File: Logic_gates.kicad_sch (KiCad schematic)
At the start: 3 parts, among them U7 MC74VHC1G04, U8 MC74VHC1G04, U9 74HC08D.653

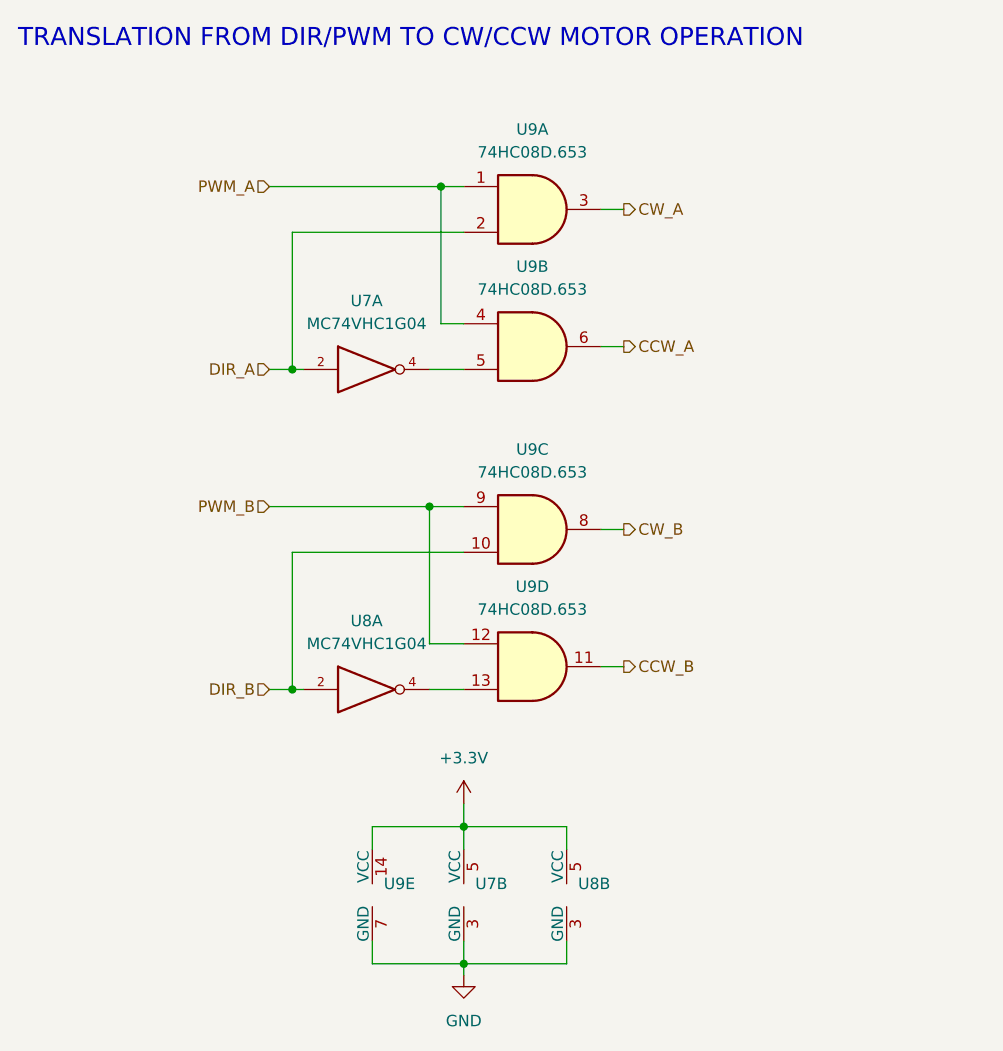
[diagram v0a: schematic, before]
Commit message: added pull-ups to the logic gates
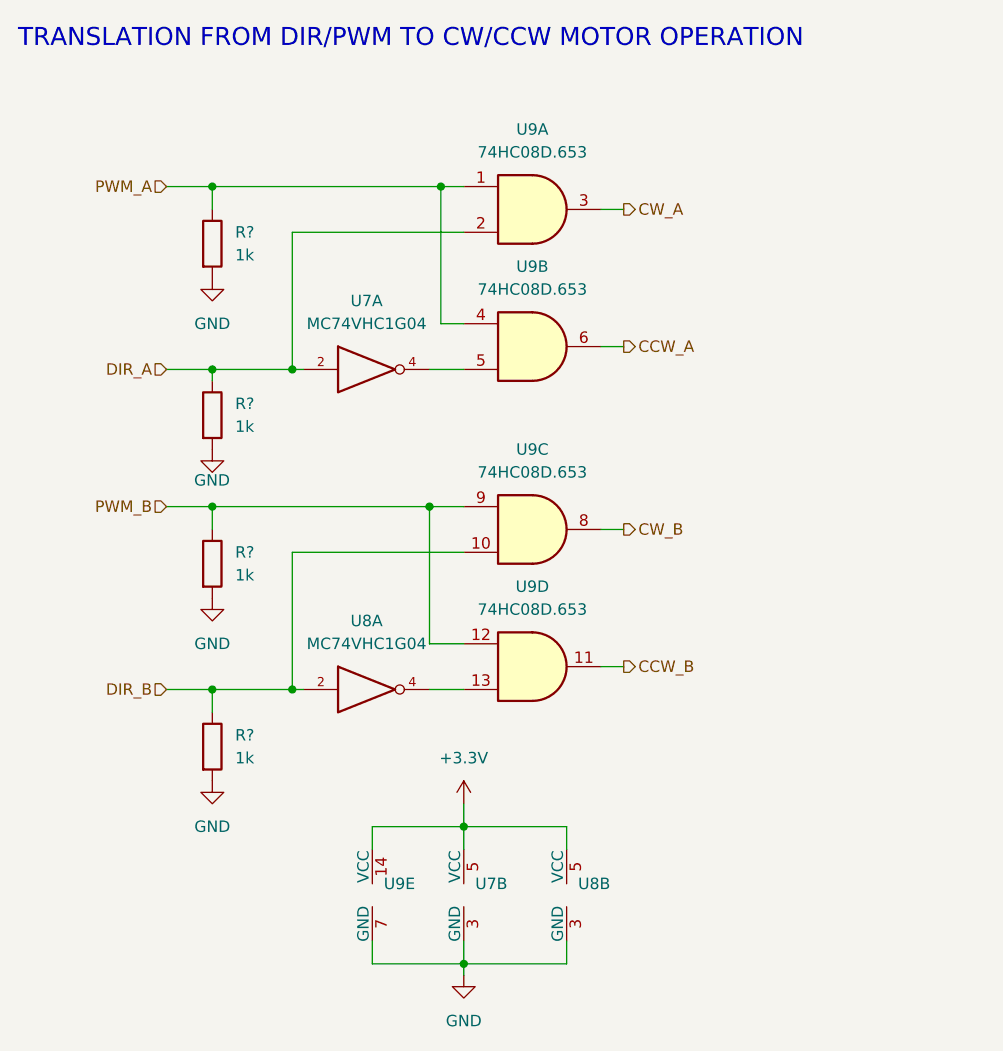
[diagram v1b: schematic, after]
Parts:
- added R? (x4): 1k, Resistor_SMD:R_0603_1608Metric_Pad0.98x0.95mm_HandSolder, symbol Device:R
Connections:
- net DIR_A: now also R?.1
- net DIR_B: now also R?.1
- net GND: now also R?.2, R?.2, R?.2, R?.2
- net PWM_A: now also R?.1
- net PWM_B: now also R?.1
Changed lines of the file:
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@@
   (junction (at 138.43 50.8) (diameter 0) (color 0 0 0 0)
   )
+  (junction (at 113.03 50.8) (diameter 0) (color 0 0 0 0)
+  )
   (junction (at 140.97 137.16) (diameter 0) (color 0 0 0 0)
   )
+  (junction (at 113.03 71.12) (diameter 0) (color 0 0 0 0)
+  )
   (junction (at 121.92 71.12) (diameter 0) (color 0 0 0 0)
   )
   (junction (at 140.97 121.92) (diameter 0) (color 0 0 0 0)
   )
+  (junction (at 113.03 86.36) (diameter 0) (color 0 0 0 0)
+  )
+  (junction (at 113.03 106.68) (diameter 0) (color 0 0 0 0)
+  )
   (junction (at 121.92 106.68) (diameter 0) (color 0 0 0 0)
   )
@@
     (stroke (width 0) (type default) (color 0 0 0 0))
   )
-  (wire (pts (xy 119.38 106.68) (xy 121.92 106.68))
+  (wire (pts (xy 107.95 106.68) (xy 113.03 106.68))
+    (stroke (width 0) (type default) (color 0 0 0 0))
+  )
+  (wire (pts (xy 113.03 106.68) (xy 121.92 106.68))
     (stroke (width 0) (type default) (color 0 0 0 0))
   )
@@
     (stroke (width 0) (type default) (color 0 0 0 0))
   )
+  (wire (pts (xy 113.03 72.39) (xy 113.03 71.12))
+    (stroke (width 0) (type default) (color 0 0 0 0))
+  )
+  (wire (pts (xy 113.03 50.8) (xy 138.43 50.8))
+    (stroke (width 0) (type default) (color 0 0 0 0))
+  )
   (wire (pts (xy 140.97 121.92) (xy 140.97 124.46))
     (stroke (width 0) (type default) (color 0 0 0 0))
@@
     (stroke (width 0) (type default) (color 0 0 0 0))
   )
+  (wire (pts (xy 113.03 71.12) (xy 121.92 71.12))
+    (stroke (width 0) (type default) (color 0 0 0 0))
+  )
   (wire (pts (xy 121.92 106.68) (xy 123.19 106.68))
     (stroke (width 0) (type default) (color 0 0 0 0))
   )
-  (wire (pts (xy 119.38 86.36) (xy 137.16 86.36))
+  (wire (pts (xy 107.95 86.36) (xy 113.03 86.36))
+    (stroke (width 0) (type default) (color 0 0 0 0))
+  )
+  (wire (pts (xy 113.03 86.36) (xy 113.03 88.9))
     (stroke (width 0) (type default) (color 0 0 0 0))
   )
@@
     (stroke (width 0) (type default) (color 0 0 0 0))
   )
+  (wire (pts (xy 113.03 106.68) (xy 113.03 109.22))
+    (stroke (width 0) (type default) (color 0 0 0 0))
+  )
   (wire (pts (xy 137.16 86.36) (xy 140.97 86.36))
     (stroke (width 0) (type default) (color 0 0 0 0))
   )
-  (wire (pts (xy 119.38 50.8) (xy 138.43 50.8))
+  (wire (pts (xy 107.95 50.8) (xy 113.03 50.8))
     (stroke (width 0) (type default) (color 0 0 0 0))
   )
@@
     (stroke (width 0) (type default) (color 0 0 0 0))
   )
-  (wire (pts (xy 119.38 71.12) (xy 121.92 71.12))
+  (wire (pts (xy 107.95 71.12) (xy 113.03 71.12))
     (stroke (width 0) (type default) (color 0 0 0 0))
   )
@@
   )
   (wire (pts (xy 130.81 124.46) (xy 130.81 121.92))
+    (stroke (width 0) (type default) (color 0 0 0 0))
+  )
+  (wire (pts (xy 113.03 50.8) (xy 113.03 53.34))
+    (stroke (width 0) (type default) (color 0 0 0 0))
+  )
+  (wire (pts (xy 113.03 86.36) (xy 137.16 86.36))
     (stroke (width 0) (type default) (color 0 0 0 0))
   )
@@
     (effects (font (size 1.27 1.27)) (justify left))
   )
-  (hierarchical_label "DIR_A" (shape input) (at 119.38 71.12 180)
+  (hierarchical_label "DIR_A" (shape input) (at 107.95 71.12 180)
     (effects (font (size 1.27 1.27)) (justify right))
   )
-  (hierarchical_label "PWM_A" (shape input) (at 119.38 50.8 180)
+  (hierarchical_label "PWM_A" (shape input) (at 107.95 50.8 180)
     (effects (font (size 1.27 1.27)) (justify right))
   )
-  (hierarchical_label "DIR_B" (shape input) (at 119.38 106.68 180)
+  (hierarchical_label "DIR_B" (shape input) (at 107.95 106.68 180)
     (effects (font (size 1.27 1.27)) (justify right))
   )
@@
     (effects (font (size 1.27 1.27)) (justify left))
   )
-  (hierarchical_label "PWM_B" (shape input) (at 119.38 86.36 180)
+  (hierarchical_label "PWM_B" (shape input) (at 107.95 86.36 180)
     (effects (font (size 1.27 1.27)) (justify right))
   )
   (hierarchical_label "CCW_A" (shape output) (at 158.75 68.58 0)
     (effects (font (size 1.27 1.27)) (justify left))
+  )
+  (symbol (lib_id "Device:R") (at 113.03 113.03 0) (unit 1)
+    (in_bom yes) (on_board yes) (fields_autoplaced)
+    (property "Reference" "R?" (id 0) (at 115.57 111.7599 0)
+      (effects (font (size 1.27 1.27)) (justify left))
+    )
+    (property "Value" "1k" (id 1) (at 115.57 114.2999 0)
+      (effects (font (size 1.27 1.27)) (justify left))
+    )
+    (property "Footprint" "Resistor_SMD:R_0603_1608Metric_Pad0.98x0.95mm_HandSolder" (id 2) (at 111.252 113.03 90)
+      (effects (font (size 1.27 1.27)) hide)
+    )
+    (property "Datasheet" "~" (id 3) (at 113.03 113.03 0)
+      (effects (font (size 1.27 1.27)) hide)
+    )
+    (pin "1")
+    (pin "2")
+  )
+  (symbol (lib_id "Device:R") (at 113.03 92.71 0) (unit 1)
+    (in_bom yes) (on_board yes) (fields_autoplaced)
+    (property "Reference" "R?" (id 0) (at 115.57 91.4399 0)
+      (effects (font (size 1.27 1.27)) (justify left))
+    )
+    (property "Value" "1k" (id 1) (at 115.57 93.9799 0)
+      (effects (font (size 1.27 1.27)) (justify left))
+    )
+    (property "Footprint" "Resistor_SMD:R_0603_1608Metric_Pad0.98x0.95mm_HandSolder" (id 2) (at 111.252 92.71 90)
+      (effects (font (size 1.27 1.27)) hide)
+    )
+    (property "Datasheet" "~" (id 3) (at 113.03 92.71 0)
+      (effects (font (size 1.27 1.27)) hide)
+    )
+    (pin "1")
+    (pin "2")
   )
   (symbol (lib_id "_IntegratedCircuits:74HC08D.653") (at 148.59 104.14 0) (unit 4)
@@
     (pin "7")
   )
+  (symbol (lib_id "Device:R") (at 113.03 57.15 0) (unit 1)
+    (in_bom yes) (on_board yes) (fields_autoplaced)
+    (property "Reference" "R?" (id 0) (at 115.57 55.8799 0)
+      (effects (font (size 1.27 1.27)) (justify left))
+    )
+    (property "Value" "1k" (id 1) (at 115.57 58.4199 0)
+      (effects (font (size 1.27 1.27)) (justify left))
+    )
+    (property "Footprint" "Resistor_SMD:R_0603_1608Metric_Pad0.98x0.95mm_HandSolder" (id 2) (at 111.252 57.15 90)
+      (effects (font (size 1.27 1.27)) hide)
+    )
+    (property "Datasheet" "~" (id 3) (at 113.03 57.15 0)
+      (effects (font (size 1.27 1.27)) hide)
+    )
+    (pin "1")
+    (pin "2")
+  )
+  (symbol (lib_id "power:GND") (at 113.03 96.52 0) (unit 1)
+    (in_bom yes) (on_board yes) (fields_autoplaced)
+    (property "Reference" "#PWR?" (id 0) (at 113.03 102.87 0)
+      (effects (font (size 1.27 1.27)) hide)
+    )
+    (property "Value" "GND" (id 1) (at 113.03 101.6 0))
+    (property "Footprint" "" (id 2) (at 113.03 96.52 0)
+      (effects (font (size 1.27 1.27)) hide)
+    )
+    (property "Datasheet" "" (id 3) (at 113.03 96.52 0)
+      (effects (font (size 1.27 1.27)) hide)
+    )
+    (pin "1")
+  )
   (symbol (lib_id "_IntegratedCircuits:MC74VHC1G04") (at 129.54 106.68 0) (unit 1)
     (in_bom yes) (on_board yes)
@@
     (pin "1")
   )
+  (symbol (lib_id "power:GND") (at 113.03 116.84 0) (unit 1)
+    (in_bom yes) (on_board yes) (fields_autoplaced)
+    (property "Reference" "#PWR?" (id 0) (at 113.03 123.19 0)
+      (effects (font (size 1.27 1.27)) hide)
+    )
+    (property "Value" "GND" (id 1) (at 113.03 121.92 0))
+    (property "Footprint" "" (id 2) (at 113.03 116.84 0)
+      (effects (font (size 1.27 1.27)) hide)
+    )
+    (property "Datasheet" "" (id 3) (at 113.03 116.84 0)
+      (effects (font (size 1.27 1.27)) hide)
+    )
+    (pin "1")
+  )
   (symbol (lib_id "_IntegratedCircuits:MC74VHC1G04") (at 129.54 71.12 0) (unit 1)
     (in_bom yes) (on_board yes) (fields_autoplaced)
@@
     (pin "3")
     (pin "5")
+  )
+  (symbol (lib_id "Device:R") (at 113.03 76.2 0) (unit 1)
+    (in_bom yes) (on_board yes) (fields_autoplaced)
+    (property "Reference" "R?" (id 0) (at 115.57 74.9299 0)
+      (effects (font (size 1.27 1.27)) (justify left))
+    )
+    (property "Value" "1k" (id 1) (at 115.57 77.4699 0)
+      (effects (font (size 1.27 1.27)) (justify left))
+    )
+    (property "Footprint" "Resistor_SMD:R_0603_1608Metric_Pad0.98x0.95mm_HandSolder" (id 2) (at 111.252 76.2 90)
+      (effects (font (size 1.27 1.27)) hide)
+    )
+    (property "Datasheet" "~" (id 3) (at 113.03 76.2 0)
+      (effects (font (size 1.27 1.27)) hide)
+    )
+    (pin "1")
+    (pin "2")
   )
   (symbol (lib_id "_IntegratedCircuits:74HC08D.653") (at 148.59 68.58 0) (unit 2)
@@
     (pin "7")
   )
+  (symbol (lib_id "power:GND") (at 113.03 60.96 0) (unit 1)
+    (in_bom yes) (on_board yes) (fields_autoplaced)
+    (property "Reference" "#PWR?" (id 0) (at 113.03 67.31 0)
+      (effects (font (size 1.27 1.27)) hide)
+    )
+    (property "Value" "GND" (id 1) (at 113.03 66.04 0))
+    (property "Footprint" "" (id 2) (at 113.03 60.96 0)
+      (effects (font (size 1.27 1.27)) hide)
+    )
+    (property "Datasheet" "" (id 3) (at 113.03 60.96 0)
+      (effects (font (size 1.27 1.27)) hide)
+    )
+    (pin "1")
+  )
   (symbol (lib_id "power:+3.3V") (at 140.97 119.38 0) (unit 1)
     (in_bom yes) (on_board yes) (fields_autoplaced)
@@
       (effects (font (size 1.27 1.27)) hide)
     )
+    (pin "1")
+  )
+  (symbol (lib_id "power:GND") (at 113.03 80.01 0) (unit 1)
+    (in_bom yes) (on_board yes)
+    (property "Reference" "#PWR?" (id 0) (at 113.03 86.36 0)
+      (effects (font (size 1.27 1.27)) hide)
+    )
+    (property "Value" "GND" (id 1) (at 112.997 83.4397 0))
+    (property "Footprint" "" (id 2) (at 113.03 80.01 0)
+      (effects (font (size 1.27 1.27)) hide)
+    )
+    (property "Datasheet" "" (id 3) (at 113.03 80.01 0)
+      (effects (font (size 1.27 1.27)) hide)
+    )

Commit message: ADC resistors and outputs added
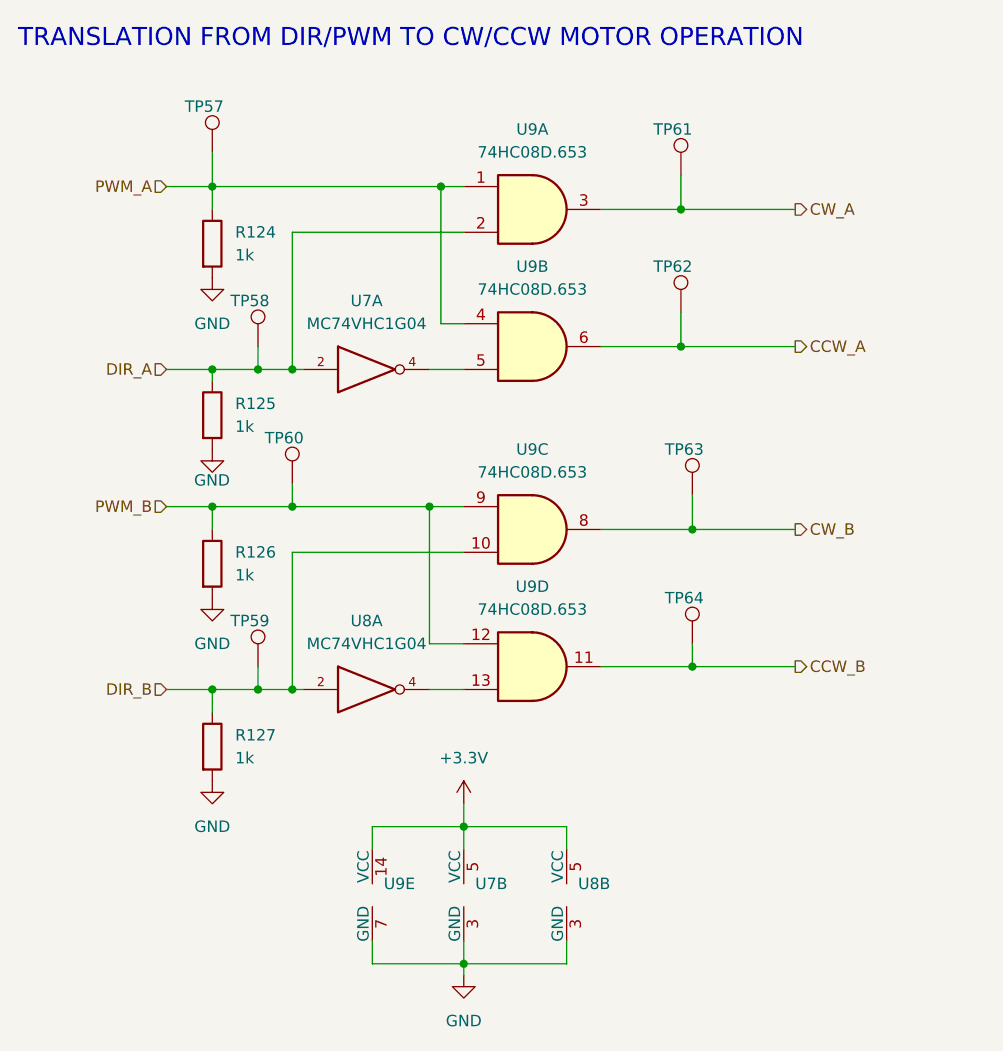
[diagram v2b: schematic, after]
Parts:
- added TP57, TP58, TP59, TP60, TP61, TP62, TP63, TP64: TestPoint, TestPoint:TestPoint_THTPad_1.0x1.0mm_Drill0.5mm, symbol Connector:TestPoint
- gave numbers to parts that had none: 4
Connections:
- net CCW_A: now also TP62.1
- net CCW_B: now also TP64.1
- net CW_A: now also TP61.1
- net CW_B: now also TP63.1
- net DIR_A: now also TP58.1
- net DIR_B: now also TP59.1
- net PWM_A: now also TP57.1
- net PWM_B: now also TP60.1
